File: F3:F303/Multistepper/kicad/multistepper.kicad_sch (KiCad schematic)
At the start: 14 parts, among them J8 USB_B, J9 Screw_Terminal_01x03, Q1 B0505S, SW3 SW_DIP_x01, U2 ISO1050DUB, U3 USBLC6-2SC6

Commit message: multistepper: cont
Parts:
- added JP1, JP2: SolderJumper_2_Bridged, Jumper:SolderJumper-2_P1.3mm_Open_TrianglePad1.0x1.5mm, symbol Jumper:SolderJumper_2_Bridged
- C10, C11: value 1 -> 1u; footprint Capacitor_SMD:C_0805_2012Metric_Pad1.15x1.40mm_HandSolder -> Capacitor_SMD:C_0603_1608Metric_Pad1.08x0.95mm_HandSolder
- Q1: footprint my_footprints:B0x0xS -> stepper:B0x0xS
- R16, R17: footprint Resistor_SMD:R_0603_1608Metric_Pad1.05x0.95mm_HandSolder -> Resistor_SMD:R_0603_1608Metric_Pad0.98x0.95mm_HandSolder
- R18: footprint Resistor_SMD:R_1210_3225Metric_Pad1.42x2.65mm_HandSolder -> Resistor_SMD:R_1210_3225Metric_Pad1.30x2.65mm_HandSolder
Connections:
- net +5V: now also JP1.1 (A), JP2.1 (A); no longer C10.1, D22.1 (K), Q1.2 (Vin), TP1.1, U2.1 (VCC1)
- new net: D22.1 (K), JP2.2 (B), TP1.1
- new net: C10.1, JP1.2 (B), Q1.2 (Vin), U2.1 (VCC1)
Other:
- moved on the sheet: C10, C11, D22, D24, J8, J9, Q1, R16, R17, R18, SW3, TP1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

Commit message: multistepper schematic
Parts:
- TP1: value 5V -> 5Vusb
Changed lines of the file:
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@@
       (effects (font (size 1.27 1.27)) (justify left))
     )
-    (property "Value" "5V" (id 1) (at 37.7952 139.7762 0)
+    (property "Value" "5Vusb" (id 1) (at 37.7952 139.7762 0)
       (effects (font (size 1.27 1.27)) (justify left) hide)
     )
@@
       (reference "#PWR03") (unit 1) (value "GND") (footprint "")
     )
-    (path "/076c38b6-e164-46bb-9d96-26f8bdfeca37/99206ade-04b2-46fa-85f1-261359dfd31b"
-      (reference "#PWR04") (unit 1) (value "+3V3") (footprint "")
-    )
     (path "/076c38b6-e164-46bb-9d96-26f8bdfeca37/f5301934-7edc-46db-ae48-58199dc2aa43"
       (reference "#PWR05") (unit 1) (value "GND") (footprint "")
@@
       (reference "#PWR08") (unit 1) (value "+3V3") (footprint "")
     )
-    (path "/076c38b6-e164-46bb-9d96-26f8bdfeca37/2b033d26-211f-47c5-ad30-9cb9aea659a6"
-      (reference "#PWR09") (unit 1) (value "+3V3") (footprint "")
-    )
-    (path "/076c38b6-e164-46bb-9d96-26f8bdfeca37/73b1df7f-a887-48b4-9ce7-3d8db7403e95"
-      (reference "#PWR010") (unit 1) (value "+3V3") (footprint "")
-    )
     (path "/076c38b6-e164-46bb-9d96-26f8bdfeca37/4d6a594b-d668-48f8-8d40-146959ef7aa5"
       (reference "#PWR011") (unit 1) (value "GND") (footprint "")
@@
       (reference "#PWR041") (unit 1) (value "GND") (footprint "")
     )
-    (path "/cf2c4fa9-a57e-4812-ae0c-3db57f6071a5/610893b8-7125-40df-867c-22854f8efd58/4f508297-4488-4315-85eb-5261f9d02134"
-      (reference "#PWR042") (unit 1) (value "+3.3V") (footprint "")
+    (path "/076c38b6-e164-46bb-9d96-26f8bdfeca37/4354a899-4f12-4b14-9a0f-0357b172479a"
+      (reference "#PWR042") (unit 1) (value "GND") (footprint "")
     )
     (path "/076c38b6-e164-46bb-9d96-26f8bdfeca37/c9d2b617-3560-41ef-a3a7-a6d08311dfc5"
@@
       (reference "#PWR0124") (unit 1) (value "GND") (footprint "")
     )
-    (path "/076c38b6-e164-46bb-9d96-26f8bdfeca37/b26d12d8-b821-4fbb-bcf0-02f1fc523839"
-      (reference "#PWR0125") (unit 1) (value "+3V3") (footprint "")
-    )
     (path "/076c38b6-e164-46bb-9d96-26f8bdfeca37/b728d2bc-216a-439f-be0d-9040aecbd583"
       (reference "C1") (unit 1) (value "12") (footprint "Capacitor_SMD:C_0603_1608Metric_Pad1.08x0.95mm_HandSolder")
@@
     )
     (path "/076c38b6-e164-46bb-9d96-26f8bdfeca37/9eb0e3e4-2412-4862-9254-ebfae0e788ab"
-      (reference "J2") (unit 1) (value "buttons_I2C") (footprint "Connector_IDC:IDC-Header_2x05_P2.54mm_Vertical")
+      (reference "J2") (unit 1) (value "Buttons/I2C") (footprint "Connector_IDC:IDC-Header_2x05_P2.54mm_Vertical")
     )
     (path "/076c38b6-e164-46bb-9d96-26f8bdfeca37/3b30193d-b3cb-42a8-a75c-e3cbeadeeead"
-      (reference "J3") (unit 1) (value "screen") (footprint "Connector_IDC:IDC-Header_2x05_P2.54mm_Vertical")
+      (reference "J3") (unit 1) (value "Screen") (footprint "Connector_IDC:IDC-Header_2x05_P2.54mm_Vertical")
     )
     (path "/beac4271-940a-4bcd-9fa5-ece775a07d41/ad1d252e-a412-4fd5-af6f-3bf5db8aac83"
@@
     )
     (path "/076c38b6-e164-46bb-9d96-26f8bdfeca37/23242767-ce55-4623-97c5-9de9c42c2a3f"
-      (reference "J7") (unit 1) (value "ADC2") (footprint "Connector_JST:JST_PH_B4B-PH-K_1x04_P2.00mm_Vertical")
+      (reference "J7") (unit 1) (value "GPO") (footprint "Connector_JST:JST_PH_B4B-PH-K_1x04_P2.00mm_Vertical")
     )
     (path "/0fd87c97-8042-4653-abdd-7019b1430685"
@@
       (reference "J10") (unit 1) (value "Screw_Terminal_01x02") (footprint "TerminalBlock_Phoenix:TerminalBlock_Phoenix_MKDS-1,5-2_1x02_P5.00mm_Horizontal")
     )
-    (path "/cf2c4fa9-a57e-4812-ae0c-3db57f6071a5/610893b8-7125-40df-867c-22854f8efd58/0f165469-1249-4064-aadf-0fc6a85a60f4"
-      (reference "J11") (unit 1) (value "Conn_01x03_Male") (footprint "Connector_PinHeader_2.54mm:PinHeader_1x03_P2.54mm_Vertical")
-    )
     (path "/cf2c4fa9-a57e-4812-ae0c-3db57f6071a5/610893b8-7125-40df-867c-22854f8efd58/0f3f2180-6e00-4de5-8d6d-bb200c241b76"
-      (reference "J12") (unit 1) (value "Conn_01x03_Male") (footprint "Connector_PinHeader_2.54mm:PinHeader_1x03_P2.54mm_Vertical")
+      (reference "J11") (unit 1) (value "LimS") (footprint "Connector_JST:JST_EH_B4B-EH-A_1x04_P2.50mm_Vertical")
     )
     (path "/cf2c4fa9-a57e-4812-ae0c-3db57f6071a5/610893b8-7125-40df-867c-22854f8efd58/e602956b-fb1a-48e1-af9c-9935214ce0ab"
-      (reference "J13") (unit 1) (value "Conn_01x04_Male") (footprint "Connector_PinHeader_2.54mm:PinHeader_1x04_P2.54mm_Vertical")
+      (reference "J12") (unit 1) (value "Stepper") (footprint "Connector_JST:JST_EH_B4B-EH-A_1x04_P2.50mm_Vertical")
+    )
+    (path "/076c38b6-e164-46bb-9d96-26f8bdfeca37/8a056ff3-5fc5-445e-813f-5479481ae2be"
+      (reference "J13") (unit 1) (value "UART") (footprint "Connector_JST:JST_PH_B3B-PH-K_1x03_P2.00mm_Vertical")
     )
     (path "/e07df136-9c14-457d-8c74-2e7051ea67ac"
@@
       (reference "JP15") (unit 1) (value "SolderJumper_2_Bridged") (footprint "Jumper:SolderJumper-2_P1.3mm_Open_TrianglePad1.0x1.5mm")
     )
-    (path "/cf2c4fa9-a57e-4812-ae0c-3db57f6071a5/610893b8-7125-40df-867c-22854f8efd58/19b709bd-064d-431e-981a-21d8140226f7"
-      (reference "JP16") (unit 1) (value "SolderJumper_2_Bridged") (footprint "Jumper:SolderJumper-2_P1.3mm_Open_TrianglePad1.0x1.5mm")
-    )
-    (path "/cf2c4fa9-a57e-4812-ae0c-3db57f6071a5/610893b8-7125-40df-867c-22854f8efd58/9a737b0c-0674-4408-94a4-2d0cb4f1ebe2"
-      (reference "JP17") (unit 1) (value "SolderJumper_2_Bridged") (footprint "Jumper:SolderJumper-2_P1.3mm_Open_TrianglePad1.0x1.5mm")
-    )
     (path "/916f71ef-9b2f-424f-a64d-0b6af99b627f/b3fc53d8-12ed-4d5b-adca-e33d10eb8430"
       (reference "L1") (unit 1) (value "100u") (footprint "Inductor_THT:L_Toroid_Horizontal_D6.5mm_P10.00mm_Diameter7-5mm_Amidon-T25")
@@
       (reference "R23") (unit 1) (value "100") (footprint "Resistor_SMD:R_0603_1608Metric_Pad0.98x0.95mm_HandSolder")
     )
+    (path "/076c38b6-e164-46bb-9d96-26f8bdfeca37/d42c91a2-1307-4ab7-930f-7f9359c5d693"
+      (reference "R24") (unit 1) (value "22") (footprint "Resistor_SMD:R_0603_1608Metric_Pad0.98x0.95mm_HandSolder")
+    )
+    (path "/076c38b6-e164-46bb-9d96-26f8bdfeca37/a8f0ad58-076a-43bc-8bc2-4c8514b9f66a"
+      (reference "R25") (unit 1) (value "22") (footprint "Resistor_SMD:R_0603_1608Metric_Pad0.98x0.95mm_HandSolder")
+    )
     (path "/076c38b6-e164-46bb-9d96-26f8bdfeca37/c2620a21-1c3d-4233-bbce-d374c7c78b67"
       (reference "RN1") (unit 1) (value "330") (footprint "Resistor_SMD:R_Array_Convex_4x0603")
@@
     )
     (path "/076c38b6-e164-46bb-9d96-26f8bdfeca37/28ab1d00-5dcf-4df3-bb52-f6a6fa59c5a0"
-      (reference "SW1") (unit 1) (value "reset") (footprint "Button_Switch_SMD:SW_SPST_FSMSM")
+      (reference "SW1") (unit 1) (value "Reset") (footprint "Button_Switch_SMD:SW_SPST_FSMSM")
     )
     (path "/076c38b6-e164-46bb-9d96-26f8bdfeca37/7c777c8b-6b38-45e7-b24d-d876b91caf36"
-      (reference "SW2") (unit 1) (value "boot") (footprint "Button_Switch_SMD:SW_SPST_FSMSM")
+      (reference "SW2") (unit 1) (value "Boot") (footprint "Button_Switch_SMD:SW_SPST_FSMSM")
     )
     (path "/b27ea6a0-a572-46ba-ba2a-053475cc4a03"
@@
     )
     (path "/fa927120-76d0-4789-86fa-35db42ec6d7f"
-      (reference "TP1") (unit 1) (value "5V") (footprint "TestPoint:TestPoint_THTPad_1.5x1.5mm_Drill0.7mm")
+      (reference "TP1") (unit 1) (value "5Vusb") (footprint "TestPoint:TestPoint_THTPad_1.5x1.5mm_Drill0.7mm")
     )
     (path "/916f71ef-9b2f-424f-a64d-0b6af99b627f/84be84b6-c711-4dd0-ad57-498504d82650"

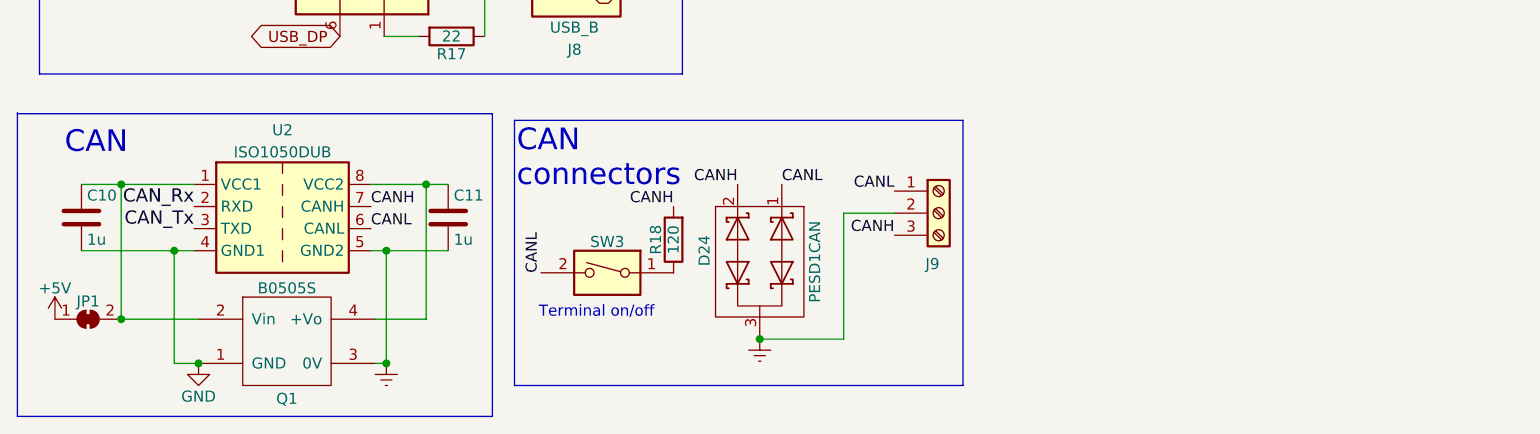
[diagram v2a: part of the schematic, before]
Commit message: Multistepper PCB almost ready
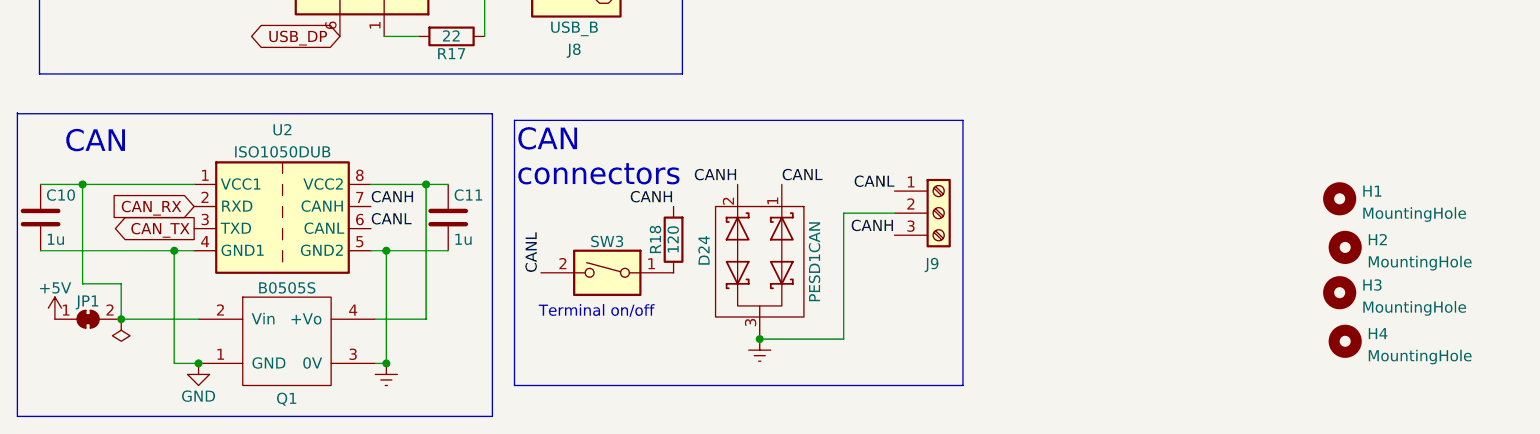
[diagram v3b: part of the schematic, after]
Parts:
- added H1, H2, H3, H4: MountingHole, MountingHole:MountingHole_3.2mm_M3_DIN965_Pad, symbol Mechanical:MountingHole
- JP1: value SolderJumper_2_Bridged -> CAN
- JP2: value SolderJumper_2_Bridged -> USB5V
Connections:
- net CAN_Rx renamed CAN_RX
- net CAN_Tx renamed CAN_TX
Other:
- moved on the sheet: C10
